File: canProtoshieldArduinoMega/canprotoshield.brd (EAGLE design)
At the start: 100 x 80 mm, 55 parts, among them CN1 1X4-3.5MM, CN10 1X4-3.5MM, CN11 1X4-3.5MM, CN12 1X4-3.5MM, CN13 1X4-3.5MM, CN14 1X4-3.5MM, CN15 1X4-3.5MM, CN16 1X4-3.5MM, CN17 1X4-3.5MM, CN18 1X4-3.5MM, CN19 1X4-3.5MM, CN2 1X4-3.5MM, CN20 1X4-3.5MM, CN21 1X4-3.5MM, CN22 1X4-3.5MM, CN23 1X4-3.5MM, CN24 1X4-3.5MM, CN25 1X4-3.5MM, CN26 1X4-3.5MM, CN27 1X4-3.5MM, CN28 1X4-3.5MM, CN29 1X4-3.5MM, CN3 1X4-3.5MM, CN30 1X4-3.5MM, CN31 1X4-3.5MM, CN32 1X4-3.5MM, CN33 1X4-3.5MM, CN34 1X4-3.5MM, CN4 1X4-3.5MM, CN5 1X4-3.5MM, CN6 1X4-3.5MM, CN7 1X4-3.5MM, CN8 1X4-3.5MM, CN9 1X4-3.5MM, U2 MCP2551, U3 ARDUINO-MEGAFULL

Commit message: Last edit need revision
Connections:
- net 10: now also CN20.3; no longer CN20.4
- net 11: now also CN20.2; no longer CN20.3
- net 12: now also CN20.1; no longer CN20.2
- net 13: no longer CN20.1
- net 2: now also CN22.3; no longer R3.2, S_CBUS.3, S_CBUS.4
- net 21: now also R3.2, S_CBUS.3, S_CBUS.4
- net 3: now also CN22.2; no longer CN22.3
- net 4: now also CN22.1; no longer CN22.2
- net 5: now also CN21.4; no longer CN22.1
- net 6: now also CN21.3; no longer CN21.4
- net 7: now also CN21.2; no longer CN21.3
- net 8: now also CN21.1; no longer CN21.2
- net 9: now also CN20.4; no longer CN21.1
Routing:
- net 21: track 0.00 -> 77.0 mm
- net N$52: track 0.00 -> 48.5 mm
- net N$31: track 0.00 -> 48.3 mm
- net 2: track 50.8 -> 10.8 mm
- net 13: track 16.5 -> 0.00 mm
- net 8: track 11.7 -> 14.6 mm
- net 4: track 9.46 -> 12.3 mm
- net 10: track 13.6 -> 16.4 mm
- net 6: track 11.4 -> 14.1 mm
- net 5: track 10.4 -> 13.1 mm
- net 7: track 12.3 -> 14.9 mm
- net 3: track 8.87 -> 11.4 mm
- net 12: track 15.6 -> 18.1 mm
- net 9: track 12.7 -> 15.2 mm
- net 11: track 14.6 -> 16.9 mm
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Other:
- board text added: "0"
- board text added: "1"
- board text added: "10"
- board text added: "11"
- board text added: "12"
- board text added: "14"
- board text added: "15"
- board text added: "16"
- board text added: "17"
- board text added: "18"
- board text added: "19"
- board text added: "2"
- board text added: "20"
- board text added: "24"
- board text added: "25"
- board text added: "27"
- board text added: "28"
- board text added: "29"
- board text added: "3"
- board text added: "30"
- board text added: "31"
- board text added: "32"
- board text added: "33"
- board text added: "34"
- board text added: "35"
- board text added: "36"
- board text added: "37"
- board text added: "38"
- board text added: "39"
- board text added: "4"
- board text added: "40"
- board text added: "41"
- board text added: "42"
- board text added: "43"
- board text added: "44"
- board text added: "45"
- board text added: "46"
- board text added: "5"
- board text added: "6"
- board text added: "7"
- board text added: "8"
- board text added: "9"
- board text added: "VCC"

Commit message: Revision
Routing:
- net MCP_SCK: track 97.9 -> 84.4 mm
- net GND: track 224.3 -> 234.5 mm
- net 28: track 23.1 -> 32.1 mm
- net 23: track 78.2 -> 85.7 mm
- net VCC: track 234.0 -> 226.6 mm, vias 2 -> 1
- net 30: track 18.6 -> 24.5 mm
- net N$2: track 11.3 -> 16.8 mm
- net MCP_SO: track 84.6 -> 81.2 mm, vias 1 -> 0
- net 42: track 20.2 -> 17.7 mm
- net 27: track 21.9 -> 24.2 mm
- net A15: track 16.7 -> 14.6 mm
- net A8: track 22.9 -> 21.3 mm
- net 48: track 21.1 -> 22.5 mm
- net 21: track 77.0 -> 78.4 mm
- net 11: track 16.9 -> 18.1 mm
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- added copper zone on layer 1, net GND
- added copper zone on layer 16, net GND
- removed copper zone on layer 16, net N$51
- removed copper zone on layer 16, net VCC

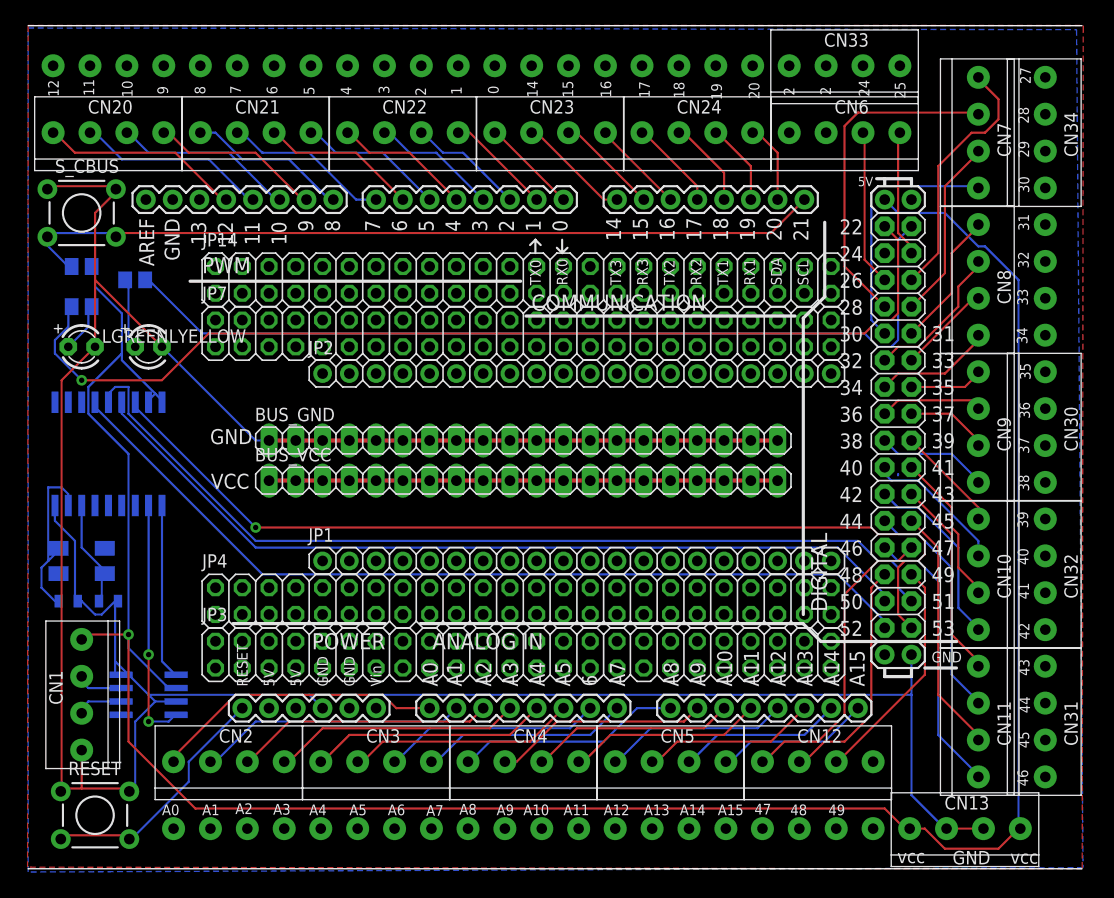
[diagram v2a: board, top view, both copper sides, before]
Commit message: Crystal change
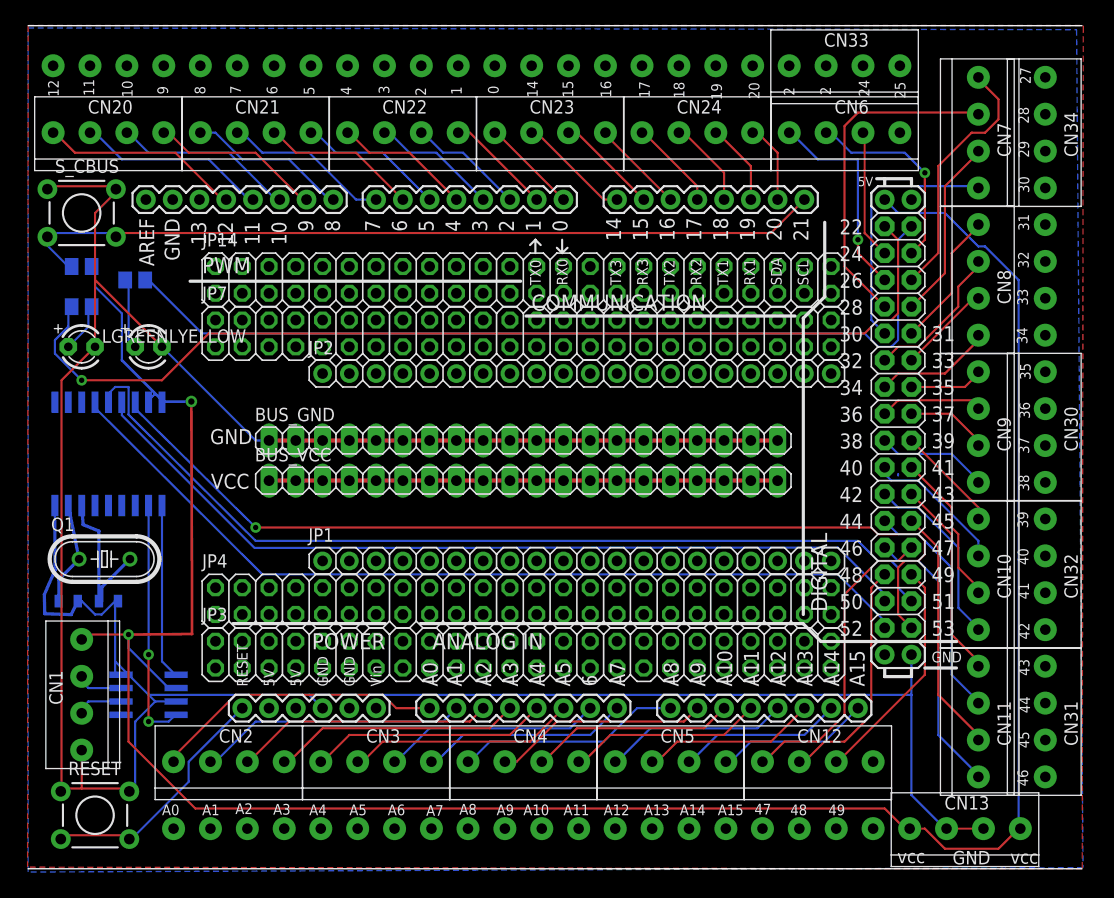
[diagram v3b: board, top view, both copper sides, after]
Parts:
- removed Q2: (no value), adafruit:CTS406
- added Q1: 16mhz, adafruit:HC49/S
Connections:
- new net N$53: CN6.4
- net 24: now also CN6.3
- net 25: now also CN6.2; no longer CN6.4
- net 26: now also CN6.1; no longer CN6.3
- net N$1: now also Q1.2; no longer Q2.3
- net N$2: now also Q1.1; no longer Q2.1
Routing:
- net 24: track 0.00 -> 12.4 mm
- net 25: track 12.1 -> 19.1 mm, vias 0 -> 1
- net N$2: track 16.8 -> 9.97 mm
- net VCC: track 226.6 -> 233.4 mm, vias 1 -> 2
- net 26: track 14.9 -> 20.1 mm, vias 0 -> 1
- net N$1: track 10.4 -> 15.4 mm
- net GND: track 234.5 -> 239.1 mm

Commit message: Made correction on the main PCB. MCP2515 had wrong connections. Added some resistor and capacitors.
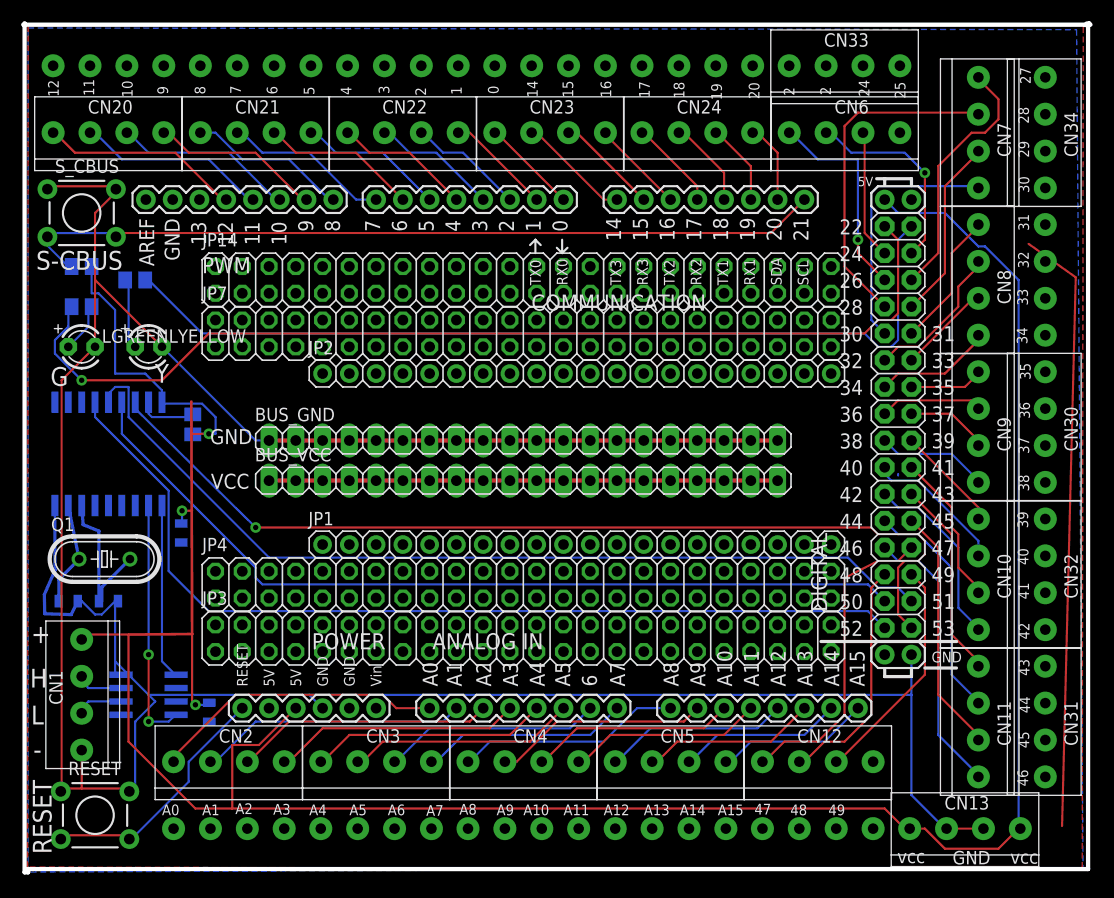
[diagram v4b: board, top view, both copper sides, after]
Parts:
- added C1, C2: 0.1uF, SparkFun-Capacitors:0805
- added R4: 10k, adafruit:M2012
- C3, C4: value 10pF -> 22pF
- moved JP4 1.56 mm to (45.7, 27.0)
- moved JP1 1.56 mm to (52.1, 30.8)
- moved JP3 1.56 mm to (45.7, 21.9)
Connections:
- new net N$54: R4.1, U$1.17
- new net N$55: U3.GND@1
- new net N$56: U3.GND@2
- net GND: now also C1.2, C2.1; no longer U2.3
- net VCC: now also C1.1, C2.2, R4.2, U3.5V@0; no longer U$1.17, U2.2
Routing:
- net VCC1: track 0.00 -> 57.6 mm
- net VCC: track 233.4 -> 253.8 mm, vias 2 -> 3
- net N$54: track 0.00 -> 5.61 mm
- net MCP_SCK: track 84.4 -> 89.1 mm
- net GND: track 239.1 -> 237.1 mm
- net MCP_SO: track 81.3 -> 82.5 mm
- net MCP_SI: track 88.3 -> 87.4 mm
- net 47: track 29.3 -> 29.9 mm
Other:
- board size 100 x 80 mm -> 101.3 x 80.6 mm
- board text added: "+"
- board text added: "-"
- board text added: "C1"
- board text added: "C2"
- board text added: "C3"
- board text added: "C4"
- board text added: "G"
- board text added: "H"
- board text added: "L"
- board text added: "R1"
- board text added: "R2"
- board text added: "R3"
- board text added: "RESET"
- board text added: "S-CBUS"
- board text added: "Y"

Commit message: New CAM files.
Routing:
- net VCC1: track 57.6 -> 0.00 mm
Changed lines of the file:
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@@
 </class>
 </classes>
-<designrules name="SparkFun">
+<designrules name="Elecrow_2-layer_eagle_rule">
+<description language="de">&lt;b&gt;EAGLE Design Rules&lt;/b&gt;
+&lt;p&gt;
+Die Standard-Design-Rules sind so gewählt, dass sie für
+die meisten Anwendungen passen. Sollte ihre Platine
+besondere Anforderungen haben, treffen Sie die erforderlichen
+Einstellungen hier und speichern die Design Rules unter
+einem neuen Namen ab.</description>
 <description language="en">&lt;b&gt;EAGLE Design Rules&lt;/b&gt;
 &lt;p&gt;
@@
 necessary adjustments and save your customized
 design rules under a new name.</description>
+<description language="zh">&lt;b&gt;Elecrow EAGLE Design Rules&lt;/b&gt;
+</description>
 <param name="layerSetup" value="(1*16)"/>
 <param name="mtCopper" value="0.035mm 0.035mm 0.035mm 0.035mm 0.035mm 0.035mm 0.035mm 0.035mm 0.035mm 0.035mm 0.035mm 0.035mm 0.035mm 0.035mm 0.035mm 0.035mm"/>
 <param name="mtIsolate" value="1.5mm 0.15mm 0.2mm 0.15mm 0.2mm 0.15mm 0.2mm 0.15mm 0.2mm 0.15mm 0.2mm 0.15mm 0.2mm 0.15mm 0.2mm"/>
-<param name="mdWireWire" value="8mil"/>
-<param name="mdWirePad" value="8mil"/>
-<param name="mdWireVia" value="8mil"/>
-<param name="mdPadPad" value="8mil"/>
-<param name="mdPadVia" value="8mil"/>
-<param name="mdViaVia" value="8mil"/>
-<param name="mdSmdPad" value="8mil"/>
-<param name="mdSmdVia" value="8mil"/>
-<param name="mdSmdSmd" value="8mil"/>
+<param name="mdWireWire" value="6mil"/>
+<param name="mdWirePad" value="6mil"/>
+<param name="mdWireVia" value="6mil"/>
+<param name="mdPadPad" value="6mil"/>
+<param name="mdPadVia" value="6mil"/>
+<param name="mdViaVia" value="6mil"/>
+<param name="mdSmdPad" value="0mil"/>
+<param name="mdSmdVia" value="0mil"/>
+<param name="mdSmdSmd" value="0mil"/>
 <param name="mdViaViaSameLayer" value="8mil"/>
 <param name="mnLayersViaInSmd" value="2"/>
 <param name="mdCopperDimension" value="10mil"/>
-<param name="mdDrill" value="8mil"/>
+<param name="mdDrill" value="10mil"/>
 <param name="mdSmdStop" value="0mil"/>
-<param name="msWidth" value="8mil"/>
-<param name="msDrill" value="20mil"/>
-<param name="msMicroVia" value="9.99mm"/>
+<param name="msWidth" value="6mil"/>
+<param name="msDrill" value="12mil"/>
+<param name="msMicroVia" value="12mil"/>
 <param name="msBlindViaRatio" value="0.5"/>
 <param name="rvPadTop" value="0.25"/>
@@
 <param name="rvMicroViaOuter" value="0.25"/>
 <param name="rvMicroViaInner" value="0.25"/>
-<param name="rlMinPadTop" value="12mil"/>
+<param name="rlMinPadTop" value="10mil"/>
 <param name="rlMaxPadTop" value="20mil"/>
 <param name="rlMinPadInner" value="10mil"/>
 <param name="rlMaxPadInner" value="20mil"/>
-<param name="rlMinPadBottom" value="12mil"/>
+<param name="rlMinPadBottom" value="10mil"/>
 <param name="rlMaxPadBottom" value="20mil"/>
-<param name="rlMinViaOuter" value="10mil"/>
+<param name="rlMinViaOuter" value="6mil"/>
 <param name="rlMaxViaOuter" value="20mil"/>
-<param name="rlMinViaInner" value="10mil"/>
+<param name="rlMinViaInner" value="6mil"/>
 <param name="rlMaxViaInner" value="20mil"/>
 <param name="rlMinMicroViaOuter" value="4mil"/>
@@
 <param name="psTop" value="-1"/>
 <param name="psBottom" value="-1"/>
-<param name="psFirst" value="-1"/>
+<param name="psFirst" value="0"/>
 <param name="psElongationLong" value="100"/>
 <param name="psElongationOffset" value="100"/>
 <param name="mvStopFrame" value="1"/>
 <param name="mvCreamFrame" value="0"/>
-<param name="mlMinStopFrame" value="4mil"/>
-<param name="mlMaxStopFrame" value="4mil"/>
+<param name="mlMinStopFrame" value="2mil"/>
+<param name="mlMaxStopFrame" value="2mil"/>
 <param name="mlMinCreamFrame" value="0mil"/>
 <param name="mlMaxCreamFrame" value="0mil"/>
-<param name="mlViaStopLimit" value="25mil"/>
+<param name="mlViaStopLimit" value="100mil"/>
 <param name="srRoundness" value="0"/>
 <param name="srMinRoundness" value="0mil"/>
@@
 <param name="checkAngle" value="0"/>
 <param name="checkFont" value="1"/>
-<param name="checkRestrict" value="1"/>
+<param name="checkRestrict" value="0"/>
 <param name="useDiameter" value="13"/>
 <param name="maxErrors" value="50"/>
@@
 <contactref element="U3" pad="GND@2"/>
 </signal>
-<signal name="VCC1">
-<wire x1="99.40944375" y1="56.1231375" x2="94.935175" y2="59.2981375" width="0.2032" layer="1"/>
-<wire x1="98.110175" y1="4.0531375" x2="99.40944375" y2="56.1231375" width="0.2032" layer="1"/>
-</signal>
 </signals>
